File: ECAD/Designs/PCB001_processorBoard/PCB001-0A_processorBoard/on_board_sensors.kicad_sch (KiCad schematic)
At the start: 21 parts, among them U3 BMI323, U4 MMC5983, U5 LG77LC

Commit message: added more connectors to the side of the PCB, added a basic power supply, and began putting parts on the PCB.
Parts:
- AE1: footprint (none) -> Connector_Coaxial:U.FL_Molex_MCRF_73412-0110_Vertical
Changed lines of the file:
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@@
 			)
 		)
-		(property "Footprint" ""
+		(property "Footprint" "Connector_Coaxial:U.FL_Molex_MCRF_73412-0110_Vertical"
 			(at 246.38 106.68 0)
 			(effects

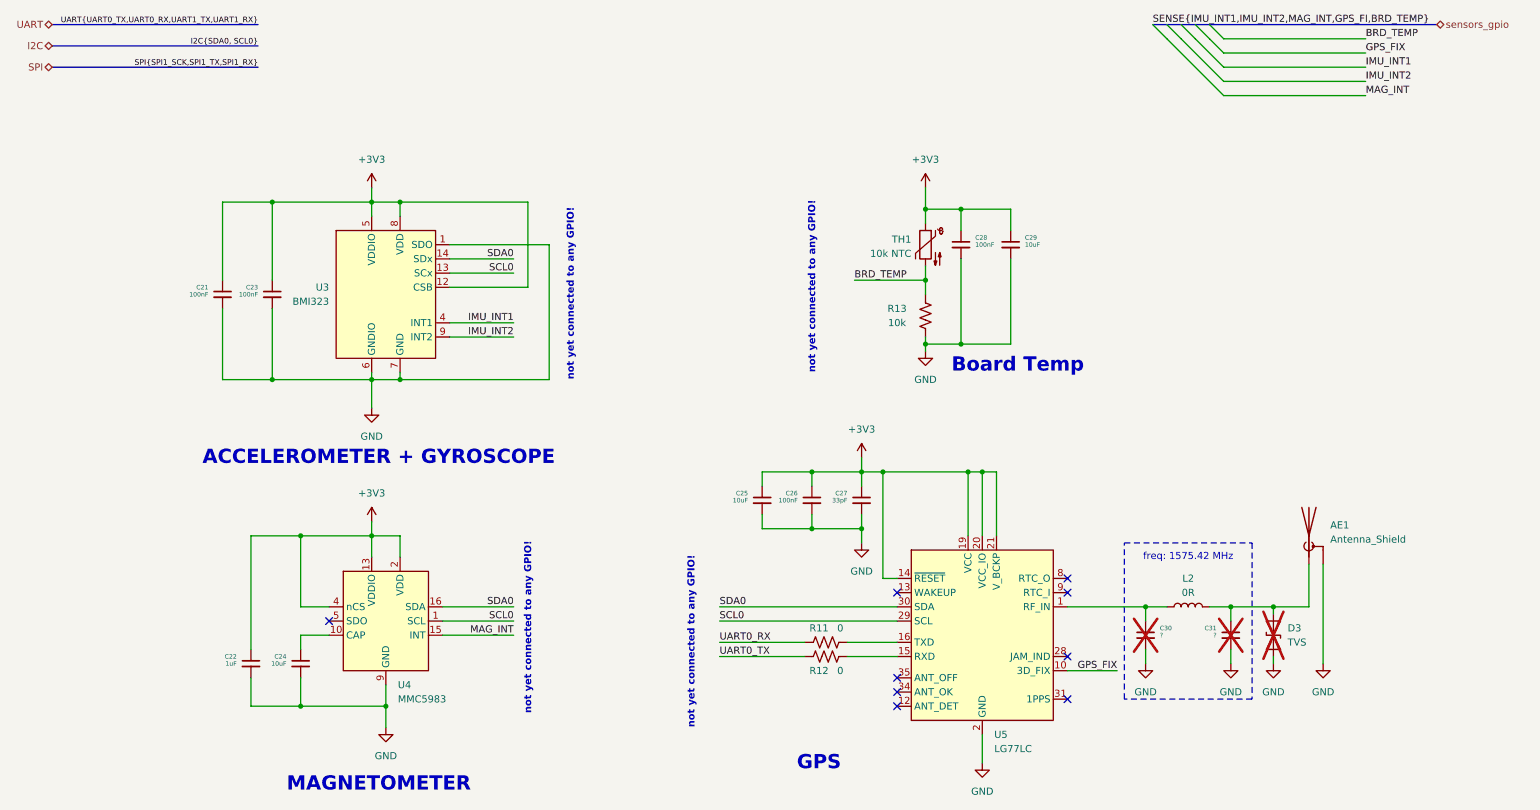
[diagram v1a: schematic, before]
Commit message: updated schematics
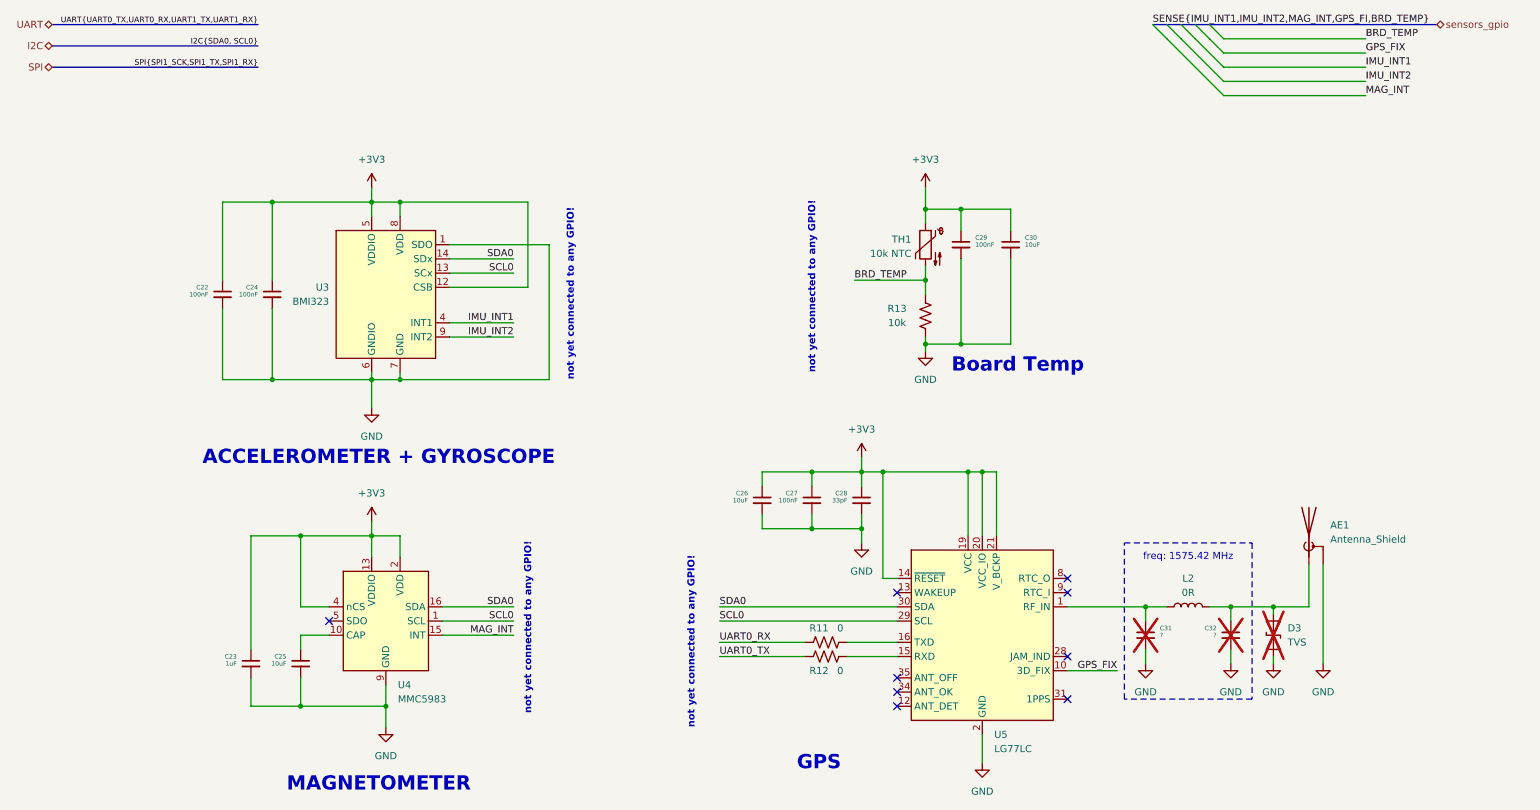
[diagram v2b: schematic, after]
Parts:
- renumbered C21 to C22, C22 to C23, C23 to C24, C24 to C25, C25 to C26, C26 to C27, C27 to C28, C28 to C29, C29 to C30, C30 to C31, C31 to C32
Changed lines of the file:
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@@
 		(dnp no)
 		(fields_autoplaced yes)
-		(property "Reference" "#PWR026"
+		(property "Reference" "#PWR027"
 			(at 78.74 92.71 0)
 			(effects
@@
 			(project ""
 				(path "/c85d256f-82d8-4180-ad51-faa565e237b8/7c839b11-0706-40ee-804c-c352a938fa7b"
-					(reference "#PWR026")
+					(reference "#PWR027")
 					(unit 1)
 				)
@@
 		(on_board yes)
 		(dnp no)
-		(property "Reference" "C23"
+		(property "Reference" "C24"
 			(at 58.42 64.7763 0)
 			(effects
@@
 			(project "PCB001-0A_processorBoard"
 				(path "/c85d256f-82d8-4180-ad51-faa565e237b8/7c839b11-0706-40ee-804c-c352a938fa7b"
-					(reference "C23")
+					(reference "C24")
 					(unit 1)
 				)
@@
 		(dnp no)
 		(fields_autoplaced yes)
-		(property "Reference" "#PWR032"
+		(property "Reference" "#PWR033"
 			(at 177.8 82.55 0)
 			(effects
@@
 			(project "PCB001-0A_processorBoard"
 				(path "/c85d256f-82d8-4180-ad51-faa565e237b8/7c839b11-0706-40ee-804c-c352a938fa7b"
-					(reference "#PWR032")
+					(reference "#PWR033")
 					(unit 1)
 				)
@@
 		(on_board yes)
 		(dnp no)
-		(property "Reference" "C24"
+		(property "Reference" "C25"
 			(at 63.5 130.8163 0)
 			(effects
@@
 			(project "PCB001-0A_processorBoard"
 				(path "/c85d256f-82d8-4180-ad51-faa565e237b8/7c839b11-0706-40ee-804c-c352a938fa7b"
-					(reference "C24")
+					(reference "C25")
 					(unit 1)
 				)
@@
 		(on_board yes)
 		(dnp no)
-		(property "Reference" "C29"
+		(property "Reference" "C30"
 			(at 195.58 55.8863 0)
 			(effects
@@
 			(project "PCB001-0A_processorBoard"
 				(path "/c85d256f-82d8-4180-ad51-faa565e237b8/7c839b11-0706-40ee-804c-c352a938fa7b"
-					(reference "C29")
+					(reference "C30")
 					(unit 1)
 				)
@@
 		(dnp no)
 		(fields_autoplaced yes)
-		(property "Reference" "#PWR037"
+		(property "Reference" "#PWR038"
 			(at 248.92 138.43 0)
 			(effects
@@
 			(project "PCB001-0A_processorBoard"
 				(path "/c85d256f-82d8-4180-ad51-faa565e237b8/7c839b11-0706-40ee-804c-c352a938fa7b"
-					(reference "#PWR037")
+					(reference "#PWR038")
 					(unit 1)
 				)
@@
 		(dnp no)
 		(fields_autoplaced yes)
-		(property "Reference" "#PWR033"
+		(property "Reference" "#PWR034"
 			(at 187.96 156.21 0)
 			(effects
@@
 			(project "PCB001-0A_processorBoard"
 				(path "/c85d256f-82d8-4180-ad51-faa565e237b8/7c839b11-0706-40ee-804c-c352a938fa7b"
-					(reference "#PWR033")
+					(reference "#PWR034")
 					(unit 1)
 				)
@@
 		(dnp no)
 		(fields_autoplaced yes)
-		(property "Reference" "#PWR027"
+		(property "Reference" "#PWR028"
 			(at 78.74 110.49 0)
 			(effects
@@
 			(project "PCB001-0A_processorBoard"
 				(path "/c85d256f-82d8-4180-ad51-faa565e237b8/7c839b11-0706-40ee-804c-c352a938fa7b"
-					(reference "#PWR027")
+					(reference "#PWR028")
 					(unit 1)
 				)
@@
 		(on_board yes)
 		(dnp no)
-		(property "Reference" "C25"
+		(property "Reference" "C26"
 			(at 146.05 101.6063 0)
 			(effects
@@
 			(project "PCB001-0A_processorBoard"
 				(path "/c85d256f-82d8-4180-ad51-faa565e237b8/7c839b11-0706-40ee-804c-c352a938fa7b"
-					(reference "C25")
+					(reference "C26")
 					(unit 1)
 				)
@@
 		(dnp no)
 		(fields_autoplaced yes)
-		(property "Reference" "#PWR030"
+		(property "Reference" "#PWR031"
 			(at 166.37 116.84 0)
 			(effects
@@
 			(project "PCB001-0A_processorBoard"
 				(path "/c85d256f-82d8-4180-ad51-faa565e237b8/7c839b11-0706-40ee-804c-c352a938fa7b"
-					(reference "#PWR030")
+					(reference "#PWR031")
 					(unit 1)
 				)
@@
 		(on_board yes)
 		(dnp no)
-		(property "Reference" "C28"
+		(property "Reference" "C29"
 			(at 186.69 55.8863 0)
 			(effects
@@
 			(project "PCB001-0A_processorBoard"
 				(path "/c85d256f-82d8-4180-ad51-faa565e237b8/7c839b11-0706-40ee-804c-c352a938fa7b"
-					(reference "C28")
+					(reference "C29")
 					(unit 1)
 				)
@@
 		(dnp no)
 		(fields_autoplaced yes)
-		(property "Reference" "#PWR028"
+		(property "Reference" "#PWR029"
 			(at 81.28 149.86 0)
 			(effects
@@
 			(project "PCB001-0A_processorBoard"
 				(path "/c85d256f-82d8-4180-ad51-faa565e237b8/7c839b11-0706-40ee-804c-c352a938fa7b"
-					(reference "#PWR028")
+					(reference "#PWR029")
 					(unit 1)
 				)
@@
 		(on_board yes)
 		(dnp yes)
-		(property "Reference" "C31"
+		(property "Reference" "C32"
 			(at 229.87 125.7363 0)
 			(effects
@@
 			(project "PCB001-0A_processorBoard"
 				(path "/c85d256f-82d8-4180-ad51-faa565e237b8/7c839b11-0706-40ee-804c-c352a938fa7b"
-					(reference "C31")
+					(reference "C32")
 					(unit 1)
 				)
@@
 		(dnp no)
 		(fields_autoplaced yes)
-		(property "Reference" "#PWR034"
+		(property "Reference" "#PWR035"
 			(at 217.17 138.43 0)
 			(effects
@@
 			(project "PCB001-0A_processorBoard"
 				(path "/c85d256f-82d8-4180-ad51-faa565e237b8/7c839b11-0706-40ee-804c-c352a938fa7b"
-					(reference "#PWR034")
+					(reference "#PWR035")
 					(unit 1)
 				)
@@
 		(dnp no)
 		(fields_autoplaced yes)
-		(property "Reference" "#PWR029"
+		(property "Reference" "#PWR030"
 			(at 166.37 99.06 0)
 			(effects
@@
 			(project "PCB001-0A_processorBoard"
 				(path "/c85d256f-82d8-4180-ad51-faa565e237b8/7c839b11-0706-40ee-804c-c352a938fa7b"
-					(reference "#PWR029")
+					(reference "#PWR030")
 					(unit 1)
 				)
@@
 		(on_board yes)
 		(dnp no)
-		(property "Reference" "C27"
+		(property "Reference" "C28"
 			(at 163.83 101.6063 0)
 			(effects
@@
 			(project "PCB001-0A_processorBoard"
 				(path "/c85d256f-82d8-4180-ad51-faa565e237b8/7c839b11-0706-40ee-804c-c352a938fa7b"
-					(reference "C27")
+					(reference "C28")
 					(unit 1)
 				)
@@
 		(on_board yes)
 		(dnp no)
-		(property "Reference" "C22"
+		(property "Reference" "C23"
 			(at 54.61 130.8163 0)
 			(effects
@@
 			(project "PCB001-0A_processorBoard"
 				(path "/c85d256f-82d8-4180-ad51-faa565e237b8/7c839b11-0706-40ee-804c-c352a938fa7b"
-					(reference "C22")
+					(reference "C23")
 					(unit 1)
 				)
@@
 		(dnp no)
 		(fields_autoplaced yes)
-		(property "Reference" "#PWR025"
+		(property "Reference" "#PWR026"
 			(at 78.74 50.8 0)
 			(effects
@@
 			(project "PCB001-0A_processorBoard"
 				(path "/c85d256f-82d8-4180-ad51-faa565e237b8/7c839b11-0706-40ee-804c-c352a938fa7b"
-					(reference "#PWR025")
+					(reference "#PWR026")
 					(unit 1)
 				)
@@
 		(dnp no)
 		(fields_autoplaced yes)
-		(property "Reference" "#PWR031"
+		(property "Reference" "#PWR032"
 			(at 177.8 50.8 0)
 			(effects
@@
 			(project "PCB001-0A_processorBoard"
 				(path "/c85d256f-82d8-4180-ad51-faa565e237b8/7c839b11-0706-40ee-804c-c352a938fa7b"
-					(reference "#PWR031")
+					(reference "#PWR032")
 					(unit 1)
 				)
@@
 		(on_board yes)
 		(dnp yes)
-		(property "Reference" "C30"
+		(property "Reference" "C31"
 			(at 219.71 125.7363 0)
 			(effects
@@
 			(project "PCB001-0A_processorBoard"
 				(path "/c85d256f-82d8-4180-ad51-faa565e237b8/7c839b11-0706-40ee-804c-c352a938fa7b"
-					(reference "C30")
+					(reference "C31")
 					(unit 1)
 				)
@@
 		(on_board yes)
 		(dnp no)
-		(property "Reference" "C21"
+		(property "Reference" "C22"
 			(at 49.53 64.7763 0)
 			(effects
@@
 			(project "PCB001-0A_processorBoard"
 				(path "/c85d256f-82d8-4180-ad51-faa565e237b8/7c839b11-0706-40ee-804c-c352a938fa7b"
-					(reference "C21")
+					(reference "C22")
 					(unit 1)
 				)
@@
 		(on_board yes)
 		(dnp no)
-		(property "Reference" "C26"
+		(property "Reference" "C27"
 			(at 154.94 101.6063 0)
 			(effects
@@
 			(project "PCB001-0A_processorBoard"
 				(path "/c85d256f-82d8-4180-ad51-faa565e237b8/7c839b11-0706-40ee-804c-c352a938fa7b"
-					(reference "C26")
+					(reference "C27")
 					(unit 1)
 				)
@@
 		(dnp no)
 		(fields_autoplaced yes)
-		(property "Reference" "#PWR036"
+		(property "Reference" "#PWR037"
 			(at 240.0266 138.4333 0)
 			(effects
@@
 			(project "PCB001-0A_processorBoard"
 				(path "/c85d256f-82d8-4180-ad51-faa565e237b8/7c839b11-0706-40ee-804c-c352a938fa7b"
-					(reference "#PWR036")
+					(reference "#PWR037")
 					(unit 1)
 				)
@@
 		(dnp no)
 		(fields_autoplaced yes)
-		(property "Reference" "#PWR035"
+		(property "Reference" "#PWR036"
 			(at 232.41 138.43 0)
 			(effects
@@
 			(project "PCB001-0A_processorBoard"
 				(path "/c85d256f-82d8-4180-ad51-faa565e237b8/7c839b11-0706-40ee-804c-c352a938fa7b"
-					(reference "#PWR035")
-					(unit 1)
-				)
+					(reference "#PWR036")
+					(unit 1)
+				)
